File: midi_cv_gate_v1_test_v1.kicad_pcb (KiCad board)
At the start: 2 copper layers, 15 x 100 mm, 26 parts, among them J1 Conn_02x05_Odd_Even, J2 Jack1, J3 Jack2, U1 LM7805_TO220, U2 TL072

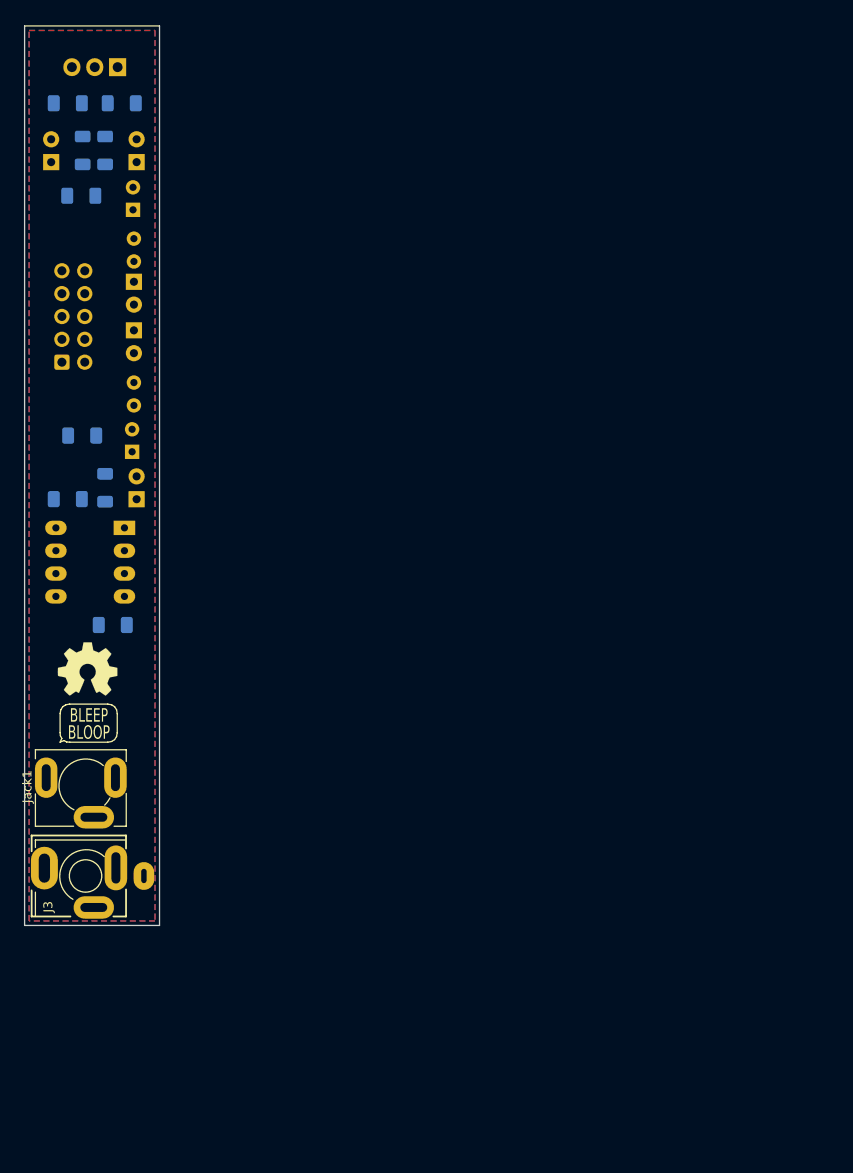
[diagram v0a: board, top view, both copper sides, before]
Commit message: Component positions first draft
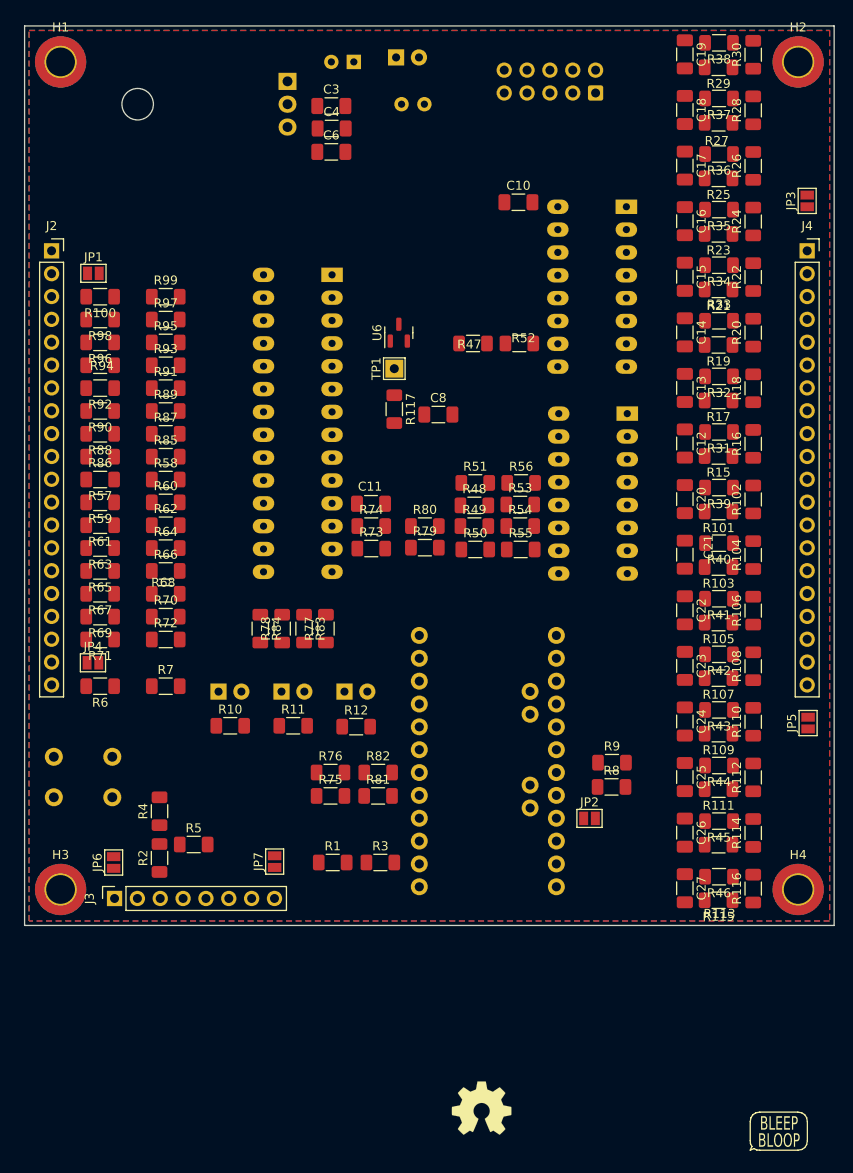
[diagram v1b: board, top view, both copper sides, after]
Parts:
- removed C2: 100uF, Capacitor_THT:CP_Radial_D5.0mm_P2.50mm
- removed C7: 10nF, Capacitor_SMD:C_1206_3216Metric_Pad1.33x1.80mm_HandSolder
- removed D2: D, Diode_THT:D_A-405_P2.54mm_Vertical_KathodeUp
- removed FB1: FerriteBead, Inductor_THT:L_Axial_L6.6mm_D2.7mm_P2.54mm_Vertical_Vishay_IM-2
- added C11: 10nF, Capacitor_SMD:C_1206_3216Metric_Pad1.33x1.80mm_HandSolder, F.Cu at (178.5, 103.1)
- added C12: 100nF, Capacitor_SMD:C_1206_3216Metric_Pad1.33x1.80mm_HandSolder, F.Cu at (213.4, 96.4)
- added C13: 100nF, Capacitor_SMD:C_1206_3216Metric_Pad1.33x1.80mm_HandSolder, F.Cu at (213.4, 90.2)
- added C14: 100nF, Capacitor_SMD:C_1206_3216Metric_Pad1.33x1.80mm_HandSolder, F.Cu at (213.4, 84.1)
- added C15: 100nF, Capacitor_SMD:C_1206_3216Metric_Pad1.33x1.80mm_HandSolder, F.Cu at (213.4, 77.9)
- added C16: 100nF, Capacitor_SMD:C_1206_3216Metric_Pad1.33x1.80mm_HandSolder, F.Cu at (213.4, 71.7)
- added C17: 100nF, Capacitor_SMD:C_1206_3216Metric_Pad1.33x1.80mm_HandSolder, F.Cu at (213.4, 65.5)
- added C18: 100nF, Capacitor_SMD:C_1206_3216Metric_Pad1.33x1.80mm_HandSolder, F.Cu at (213.4, 59.3)
- added C19: 100nF, Capacitor_SMD:C_1206_3216Metric_Pad1.33x1.80mm_HandSolder, F.Cu at (213.4, 53.2)
- added C20: 100nF, Capacitor_SMD:C_1206_3216Metric_Pad1.33x1.80mm_HandSolder, F.Cu at (213.4, 102.6)
- added C21: 100nF, Capacitor_SMD:C_1206_3216Metric_Pad1.33x1.80mm_HandSolder, F.Cu at (213.4, 108.8)
- added C22: 100nF, Capacitor_SMD:C_1206_3216Metric_Pad1.33x1.80mm_HandSolder, F.Cu at (213.4, 115.0)
- added C23: 100nF, Capacitor_SMD:C_1206_3216Metric_Pad1.33x1.80mm_HandSolder, F.Cu at (213.4, 121.1)
- added C24: 100nF, Capacitor_SMD:C_1206_3216Metric_Pad1.33x1.80mm_HandSolder, F.Cu at (213.4, 127.3)
- added C25: 100nF, Capacitor_SMD:C_1206_3216Metric_Pad1.33x1.80mm_HandSolder, F.Cu at (213.4, 133.5)
- added C26: 100nF, Capacitor_SMD:C_1206_3216Metric_Pad1.33x1.80mm_HandSolder, F.Cu at (213.4, 139.7)
- added C27: 100nF, Capacitor_SMD:C_1206_3216Metric_Pad1.33x1.80mm_HandSolder, F.Cu at (213.4, 145.9)
- added H1: MountingHole_Pad, MountingHole:MountingHole_3.2mm_M3_ISO7380_Pad_TopBottom, F.Cu at (144.0, 54.0)
- added H2: MountingHole_Pad, MountingHole:MountingHole_3.2mm_M3_ISO7380_Pad_TopBottom, F.Cu at (226.0, 54.0)
- added H3: MountingHole_Pad, MountingHole:MountingHole_3.2mm_M3_ISO7380_Pad_TopBottom, F.Cu at (144.0, 146.0)
- added H4: MountingHole_Pad, MountingHole:MountingHole_3.2mm_M3_ISO7380_Pad_TopBottom, F.Cu at (226.0, 146.0)
- added J4: Conn_01x20, Connector_PinSocket_2.54mm:PinSocket_1x20_P2.54mm_Vertical, F.Cu at (227.0, 75.0)
- added JP1: Jumper_2_Open, Jumper:SolderJumper-2_P1.3mm_Open_Pad1.0x1.5mm, F.Cu at (147.7, 77.5)
- added JP2: Jumper_2_Open, Jumper:SolderJumper-2_P1.3mm_Open_Pad1.0x1.5mm, F.Cu at (202.8, 138.1)
- added JP3: Jumper_2_Open, Jumper:SolderJumper-2_P1.3mm_Open_Pad1.0x1.5mm, F.Cu at (227.0, 69.5)
- added JP4: Jumper_2_Open, Jumper:SolderJumper-2_P1.3mm_Open_Pad1.0x1.5mm, F.Cu at (147.6, 120.8)
- added JP5: Jumper_2_Open, Jumper:SolderJumper-2_P1.3mm_Open_Pad1.0x1.5mm, F.Cu at (227.1, 127.5)
- added JP6: Jumper_2_Open, Jumper:SolderJumper-2_P1.3mm_Open_Pad1.0x1.5mm, F.Cu at (149.9, 143.0)
- added JP7: Jumper_2_Open, Jumper:SolderJumper-2_P1.3mm_Open_Pad1.0x1.5mm, F.Cu at (167.8, 142.9)
- added R10: 1k, Resistor_SMD:R_1206_3216Metric_Pad1.30x1.75mm_HandSolder, F.Cu at (162.9, 127.8)
- added R100: 10k, Resistor_SMD:R_1206_3216Metric_Pad1.30x1.75mm_HandSolder, F.Cu at (148.4, 80.1)
- added R101: 10k, Resistor_SMD:R_1206_3216Metric_Pad1.30x1.75mm_HandSolder, F.Cu at (217.2, 104.0)
- added R102: 10k, Resistor_SMD:R_1206_3216Metric_Pad1.30x1.75mm_HandSolder, F.Cu at (221.0, 102.6)
- added R103: 10k, Resistor_SMD:R_1206_3216Metric_Pad1.30x1.75mm_HandSolder, F.Cu at (217.2, 110.2)
- added R104: 10k, Resistor_SMD:R_1206_3216Metric_Pad1.30x1.75mm_HandSolder, F.Cu at (221.0, 108.8)
- added R105: 10k, Resistor_SMD:R_1206_3216Metric_Pad1.30x1.75mm_HandSolder, F.Cu at (217.2, 116.3)
- added R106: 10k, Resistor_SMD:R_1206_3216Metric_Pad1.30x1.75mm_HandSolder, F.Cu at (221.0, 115.0)
- added R107: 10k, Resistor_SMD:R_1206_3216Metric_Pad1.30x1.75mm_HandSolder, F.Cu at (217.2, 122.5)
- added R108: 10k, Resistor_SMD:R_1206_3216Metric_Pad1.30x1.75mm_HandSolder, F.Cu at (221.0, 121.2)
- added R109: 10k, Resistor_SMD:R_1206_3216Metric_Pad1.30x1.75mm_HandSolder, F.Cu at (217.2, 128.7)
- added R11: 1k, Resistor_SMD:R_1206_3216Metric_Pad1.30x1.75mm_HandSolder, F.Cu at (169.9, 127.8)
- added R110: 10k, Resistor_SMD:R_1206_3216Metric_Pad1.30x1.75mm_HandSolder, F.Cu at (221.0, 127.4)
- added R111: 10k, Resistor_SMD:R_1206_3216Metric_Pad1.30x1.75mm_HandSolder, F.Cu at (217.2, 134.9)
- added R112: 10k, Resistor_SMD:R_1206_3216Metric_Pad1.30x1.75mm_HandSolder, F.Cu at (221.0, 133.5)
- added R113: 10k, Resistor_SMD:R_1206_3216Metric_Pad1.30x1.75mm_HandSolder, F.Cu at (217.2, 141.0)
- added R114: 10k, Resistor_SMD:R_1206_3216Metric_Pad1.30x1.75mm_HandSolder, F.Cu at (221.0, 139.7)
- added R115: 10k, Resistor_SMD:R_1206_3216Metric_Pad1.30x1.75mm_HandSolder, F.Cu at (217.2, 147.2)
- added R116: 10k, Resistor_SMD:R_1206_3216Metric_Pad1.30x1.75mm_HandSolder, F.Cu at (221.0, 145.9)
- added R117: 10k, Resistor_SMD:R_1206_3216Metric_Pad1.30x1.75mm_HandSolder, F.Cu at (181.1, 92.6)
- added R12: 1k, Resistor_SMD:R_1206_3216Metric_Pad1.30x1.75mm_HandSolder, F.Cu at (176.9, 127.9)
- added R15: 10k, Resistor_SMD:R_1206_3216Metric_Pad1.30x1.75mm_HandSolder, F.Cu at (217.2, 97.8)
- added R16: 10k, Resistor_SMD:R_1206_3216Metric_Pad1.30x1.75mm_HandSolder, F.Cu at (221.0, 96.5)
- added R17: 10k, Resistor_SMD:R_1206_3216Metric_Pad1.30x1.75mm_HandSolder, F.Cu at (217.2, 91.6)
- added R18: 10k, Resistor_SMD:R_1206_3216Metric_Pad1.30x1.75mm_HandSolder, F.Cu at (221.0, 90.3)
- added R19: 10k, Resistor_SMD:R_1206_3216Metric_Pad1.30x1.75mm_HandSolder, F.Cu at (217.2, 85.5)
- added R20: 10k, Resistor_SMD:R_1206_3216Metric_Pad1.30x1.75mm_HandSolder, F.Cu at (221.0, 84.1)
- added R21: 10k, Resistor_SMD:R_1206_3216Metric_Pad1.30x1.75mm_HandSolder, F.Cu at (217.2, 79.3)
- added R22: 10k, Resistor_SMD:R_1206_3216Metric_Pad1.30x1.75mm_HandSolder, F.Cu at (221.0, 77.9)
- added R23: 10k, Resistor_SMD:R_1206_3216Metric_Pad1.30x1.75mm_HandSolder, F.Cu at (217.2, 73.1)
- added R24: 10k, Resistor_SMD:R_1206_3216Metric_Pad1.30x1.75mm_HandSolder, F.Cu at (221.0, 71.7)
- added R25: 10k, Resistor_SMD:R_1206_3216Metric_Pad1.30x1.75mm_HandSolder, F.Cu at (217.2, 66.9)
- added R26: 10k, Resistor_SMD:R_1206_3216Metric_Pad1.30x1.75mm_HandSolder, F.Cu at (221.0, 65.6)
- added R27: 10k, Resistor_SMD:R_1206_3216Metric_Pad1.30x1.75mm_HandSolder, F.Cu at (217.2, 60.8)
- added R28: 10k, Resistor_SMD:R_1206_3216Metric_Pad1.30x1.75mm_HandSolder, F.Cu at (221.0, 59.4)
- added R29: 10k, Resistor_SMD:R_1206_3216Metric_Pad1.30x1.75mm_HandSolder, F.Cu at (217.2, 54.6)
- added R30: 10k, Resistor_SMD:R_1206_3216Metric_Pad1.30x1.75mm_HandSolder, F.Cu at (221.0, 53.2)
- added R31: 330, Resistor_SMD:R_1206_3216Metric_Pad1.30x1.75mm_HandSolder, F.Cu at (217.2, 95.1)
- added R32: 330, Resistor_SMD:R_1206_3216Metric_Pad1.30x1.75mm_HandSolder, F.Cu at (217.2, 89.0)
- added R33: 330, Resistor_SMD:R_1206_3216Metric_Pad1.30x1.75mm_HandSolder, F.Cu at (217.2, 82.8)
- added R34: 330, Resistor_SMD:R_1206_3216Metric_Pad1.30x1.75mm_HandSolder, F.Cu at (217.2, 76.6)
- added R35: 330, Resistor_SMD:R_1206_3216Metric_Pad1.30x1.75mm_HandSolder, F.Cu at (217.2, 70.4)
- added R36: 330, Resistor_SMD:R_1206_3216Metric_Pad1.30x1.75mm_HandSolder, F.Cu at (217.2, 64.2)
- added R37: 330, Resistor_SMD:R_1206_3216Metric_Pad1.30x1.75mm_HandSolder, F.Cu at (217.2, 58.1)
- added R38: 330, Resistor_SMD:R_1206_3216Metric_Pad1.30x1.75mm_HandSolder, F.Cu at (217.2, 51.9)
- added R39: 330, Resistor_SMD:R_1206_3216Metric_Pad1.30x1.75mm_HandSolder, F.Cu at (217.2, 101.3)
- added R4: 10k, Resistor_SMD:R_1206_3216Metric_Pad1.30x1.75mm_HandSolder, F.Cu at (155.0, 137.3)
- added R40: 330, Resistor_SMD:R_1206_3216Metric_Pad1.30x1.75mm_HandSolder, F.Cu at (217.2, 107.5)
- added R41: 330, Resistor_SMD:R_1206_3216Metric_Pad1.30x1.75mm_HandSolder, F.Cu at (217.2, 113.7)
- added R42: 330, Resistor_SMD:R_1206_3216Metric_Pad1.30x1.75mm_HandSolder, F.Cu at (217.2, 119.9)
- added R43: 330, Resistor_SMD:R_1206_3216Metric_Pad1.30x1.75mm_HandSolder, F.Cu at (217.2, 126.0)
- added R44: 330, Resistor_SMD:R_1206_3216Metric_Pad1.30x1.75mm_HandSolder, F.Cu at (217.2, 132.2)
- added R45: 330, Resistor_SMD:R_1206_3216Metric_Pad1.30x1.75mm_HandSolder, F.Cu at (217.2, 138.4)
- added R46: 330, Resistor_SMD:R_1206_3216Metric_Pad1.30x1.75mm_HandSolder, F.Cu at (217.2, 144.6)
- added R47: 10k, Resistor_SMD:R_1206_3216Metric_Pad1.30x1.75mm_HandSolder, F.Cu at (189.8, 85.3)
- added R48: 10k, Resistor_SMD:R_1206_3216Metric_Pad1.30x1.75mm_HandSolder, F.Cu at (190.0, 103.3)
- added R49: 10k, Resistor_SMD:R_1206_3216Metric_Pad1.30x1.75mm_HandSolder, F.Cu at (190.0, 105.6)
- added R5: 10k, Resistor_SMD:R_1206_3216Metric_Pad1.30x1.75mm_HandSolder, F.Cu at (158.8, 141.0)
- added R50: 10k, Resistor_SMD:R_1206_3216Metric_Pad1.30x1.75mm_HandSolder, F.Cu at (190.1, 108.2)
- added R51: 10k, Resistor_SMD:R_1206_3216Metric_Pad1.30x1.75mm_HandSolder, F.Cu at (190.1, 100.8)
- added R52: 10k, Resistor_SMD:R_1206_3216Metric_Pad1.30x1.75mm_HandSolder, F.Cu at (195.0, 85.3)
- added R53: 10k, Resistor_SMD:R_1206_3216Metric_Pad1.30x1.75mm_HandSolder, F.Cu at (195.1, 103.2)
- added R54: 10k, Resistor_SMD:R_1206_3216Metric_Pad1.30x1.75mm_HandSolder, F.Cu at (195.1, 105.6)
- added R55: 10k, Resistor_SMD:R_1206_3216Metric_Pad1.30x1.75mm_HandSolder, F.Cu at (195.2, 108.2)
- added R56: 10k, Resistor_SMD:R_1206_3216Metric_Pad1.30x1.75mm_HandSolder, F.Cu at (195.2, 100.8)
- added R57: 10k, Resistor_SMD:R_1206_3216Metric_Pad1.30x1.75mm_HandSolder, F.Cu at (148.4, 100.4)
- added R58: 10k, Resistor_SMD:R_1206_3216Metric_Pad1.30x1.75mm_HandSolder, F.Cu at (155.7, 100.4)
- added R59: 10k, Resistor_SMD:R_1206_3216Metric_Pad1.30x1.75mm_HandSolder, F.Cu at (148.4, 103.0)
- added R6: 10k, Resistor_SMD:R_1206_3216Metric_Pad1.30x1.75mm_HandSolder, F.Cu at (148.4, 123.4)
- added R60: 10k, Resistor_SMD:R_1206_3216Metric_Pad1.30x1.75mm_HandSolder, F.Cu at (155.7, 103.0)
- added R61: 10k, Resistor_SMD:R_1206_3216Metric_Pad1.30x1.75mm_HandSolder, F.Cu at (148.4, 105.5)
- added R62: 10k, Resistor_SMD:R_1206_3216Metric_Pad1.30x1.75mm_HandSolder, F.Cu at (155.7, 105.5)
- added R63: 10k, Resistor_SMD:R_1206_3216Metric_Pad1.30x1.75mm_HandSolder, F.Cu at (148.4, 108.0)
- added R64: 10k, Resistor_SMD:R_1206_3216Metric_Pad1.30x1.75mm_HandSolder, F.Cu at (155.7, 108.0)
- added R65: 10k, Resistor_SMD:R_1206_3216Metric_Pad1.30x1.75mm_HandSolder, F.Cu at (148.4, 110.6)
- added R66: 10k, Resistor_SMD:R_1206_3216Metric_Pad1.30x1.75mm_HandSolder, F.Cu at (155.7, 110.6)
- added R67: 10k, Resistor_SMD:R_1206_3216Metric_Pad1.30x1.75mm_HandSolder, F.Cu at (148.4, 113.1)
- added R68: 10k, Resistor_SMD:R_1206_3216Metric_Pad1.30x1.75mm_HandSolder, F.Cu at (155.7, 113.1)
- added R69: 10k, Resistor_SMD:R_1206_3216Metric_Pad1.30x1.75mm_HandSolder, F.Cu at (148.4, 115.7)
- added R7: 10k, Resistor_SMD:R_1206_3216Metric_Pad1.30x1.75mm_HandSolder, F.Cu at (155.7, 123.4)
- added R70: 10k, Resistor_SMD:R_1206_3216Metric_Pad1.30x1.75mm_HandSolder, F.Cu at (155.7, 115.7)
- added R71: 10k, Resistor_SMD:R_1206_3216Metric_Pad1.30x1.75mm_HandSolder, F.Cu at (148.4, 118.2)
- added R72: 10k, Resistor_SMD:R_1206_3216Metric_Pad1.30x1.75mm_HandSolder, F.Cu at (155.7, 118.2)
- added R73: 10k, Resistor_SMD:R_1206_3216Metric_Pad1.30x1.75mm_HandSolder, F.Cu at (178.5, 108.1)
- added R74: 10k, Resistor_SMD:R_1206_3216Metric_Pad1.30x1.75mm_HandSolder, F.Cu at (178.5, 105.6)
- added R75: 10k, Resistor_SMD:R_1206_3216Metric_Pad1.30x1.75mm_HandSolder, F.Cu at (174.0, 135.6)
- added R76: 10k, Resistor_SMD:R_1206_3216Metric_Pad1.30x1.75mm_HandSolder, F.Cu at (174.0, 133.0)
- added R77: 10k, Resistor_SMD:R_1206_3216Metric_Pad1.30x1.75mm_HandSolder, F.Cu at (173.5, 117.0)
- added R78: 10k, Resistor_SMD:R_1206_3216Metric_Pad1.30x1.75mm_HandSolder, F.Cu at (168.6, 117.0)
- added R79: 10k, Resistor_SMD:R_1206_3216Metric_Pad1.30x1.75mm_HandSolder, F.Cu at (184.5, 108.0)
- added R8: 10k, Resistor_SMD:R_1206_3216Metric_Pad1.30x1.75mm_HandSolder, F.Cu at (205.2, 134.6)
- added R80: 10k, Resistor_SMD:R_1206_3216Metric_Pad1.30x1.75mm_HandSolder, F.Cu at (184.5, 105.6)
- added R81: 10k, Resistor_SMD:R_1206_3216Metric_Pad1.30x1.75mm_HandSolder, F.Cu at (179.3, 135.6)
- added R82: 10k, Resistor_SMD:R_1206_3216Metric_Pad1.30x1.75mm_HandSolder, F.Cu at (179.3, 133.0)
- added R83: 10k, Resistor_SMD:R_1206_3216Metric_Pad1.30x1.75mm_HandSolder, F.Cu at (171.1, 117.0)
- added R84: 10k, Resistor_SMD:R_1206_3216Metric_Pad1.30x1.75mm_HandSolder, F.Cu at (166.2, 117.0)
- added R85: 10k, Resistor_SMD:R_1206_3216Metric_Pad1.30x1.75mm_HandSolder, F.Cu at (155.7, 97.9)
- added R86: 10k, Resistor_SMD:R_1206_3216Metric_Pad1.30x1.75mm_HandSolder, F.Cu at (148.4, 97.9)
- added R87: 10k, Resistor_SMD:R_1206_3216Metric_Pad1.30x1.75mm_HandSolder, F.Cu at (155.7, 95.3)
- added R88: 10k, Resistor_SMD:R_1206_3216Metric_Pad1.30x1.75mm_HandSolder, F.Cu at (148.4, 95.3)
- added R89: 10k, Resistor_SMD:R_1206_3216Metric_Pad1.30x1.75mm_HandSolder, F.Cu at (155.7, 92.8)
- added R9: 10k, Resistor_SMD:R_1206_3216Metric_Pad1.30x1.75mm_HandSolder, F.Cu at (205.3, 131.9)
- added R90: 10k, Resistor_SMD:R_1206_3216Metric_Pad1.30x1.75mm_HandSolder, F.Cu at (148.4, 92.8)
- added R91: 10k, Resistor_SMD:R_1206_3216Metric_Pad1.30x1.75mm_HandSolder, F.Cu at (155.7, 90.3)
- added R92: 10k, Resistor_SMD:R_1206_3216Metric_Pad1.30x1.75mm_HandSolder, F.Cu at (148.4, 90.3)
- added R93: 10k, Resistor_SMD:R_1206_3216Metric_Pad1.30x1.75mm_HandSolder, F.Cu at (155.7, 87.7)
- added R94: 10k, Resistor_SMD:R_1206_3216Metric_Pad1.30x1.75mm_HandSolder, F.Cu at (148.4, 87.7)
- added R95: 10k, Resistor_SMD:R_1206_3216Metric_Pad1.30x1.75mm_HandSolder, F.Cu at (155.7, 85.2)
- added R96: 10k, Resistor_SMD:R_1206_3216Metric_Pad1.30x1.75mm_HandSolder, F.Cu at (148.4, 85.2)
- added R97: 10k, Resistor_SMD:R_1206_3216Metric_Pad1.30x1.75mm_HandSolder, F.Cu at (155.7, 82.6)
- added R98: 10k, Resistor_SMD:R_1206_3216Metric_Pad1.30x1.75mm_HandSolder, F.Cu at (148.4, 82.6)
- added R99: 10k, Resistor_SMD:R_1206_3216Metric_Pad1.30x1.75mm_HandSolder, F.Cu at (155.7, 80.1)
- added SW_RESET1: SW_Push, Button_Switch_THT:SW_PUSH_6mm_H5mm, B.Cu at (149.8, 131.2)
- added TP1: TestPoint, TestPoint:TestPoint_THTPad_2.0x2.0mm_Drill1.0mm, F.Cu at (181.1, 88.1)
- added U3: MCP3208, Package_DIP:DIP-16_W7.62mm_Socket_LongPads, B.Cu at (206.9, 70.1)
- added U4: MCP3208, Package_DIP:DIP-16_W7.62mm_Socket_LongPads, B.Cu at (207.0, 93.1)
- added U5: MCP23018_SP, Package_DIP:DIP-28_W7.62mm_Socket_LongPads, B.Cu at (174.2, 77.7)
- added U6: LM4040DBZ-5, Package_TO_SOT_SMD:SOT-23, F.Cu at (181.6, 84.1)
- C10: renamed from C5; value 10nF -> 100nF; moved to F.Cu
- C3, C4, C6: moved to F.Cu
- C8: value 10nF -> 100nF; moved to F.Cu
- D1: value +12_LED -> +5_LED
- D4: value -12_LED -> +5_LED
- J2: value Jack1 -> Conn_01x20; footprint My Stuff:Jack_3.5mm_MJ-355W_Vertical -> Connector_PinSocket_2.54mm:PinSocket_1x20_P2.54mm_Vertical
- J3: value Jack2 -> Conn_01x08; footprint My Stuff:Jack_3.5mm_MJ-355W_and_PJ398SM_Vertical -> Connector_PinSocket_2.54mm:PinSocket_1x08_P2.54mm_Vertical
- R1, R2, R3: value R -> 10k; moved to F.Cu
- U1: footprint Package_TO_SOT_THT:TO-220-3_Vertical -> Package_TO_SOT_THT:TO-220-3_Horizontal_TabDown
- U2: value TL072 -> ARDUINO_PRO_MINI_custom_2; footprint Package_DIP:DIP-8_W7.62mm_Socket_LongPads -> My Stuff:MODULE_ARDUINO_PRO_MINI_custom_2
- moved LOGO1 89.1 mm to (223.8, 172.9)
- moved LOGO2 89.1 mm to (223.8, 172.9)
- moved R3 85.8 mm to (179.6, 143.0), turned to 0 degrees
- moved R1 83.1 mm to (174.2, 143.0), turned to 0 degrees
- moved D5 67.3 mm to (175.6, 124.0), turned to 0 degrees
- moved J1 66.5 mm to (203.5, 57.5), turned to 90 degrees
- moved LOGO3 65.6 mm to (190.8, 170.3)
- moved J2 59.6 mm to (143.0, 75.0), turned to 0 degrees
- moved D1 59.6 mm to (161.6, 124.0), turned to 0 degrees
- moved C10 55.0 mm to (194.9, 69.6), turned to 0 degrees
- moved U2 48.7 mm to (191.5, 133.0), turned to 0 degrees
- moved C8 43.1 mm to (186.0, 93.2)
- moved R2 41.6 mm to (155.0, 142.5)
- moved D3 38.4 mm to (181.3, 53.5), turned to 0 degrees
- moved FB2 33.3 mm to (181.9, 58.7), turned to 0 degrees
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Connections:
- C10 pad 2: -12V -> +5V
- C8 pad 2: -12V -> +5V
- D1 pad 2: +12V -> Net-(D1-Pad2)
- D4 pad 2: GND -> Net-(D4-Pad2)
- D5 pad 2: +5V -> Net-(D5-Pad2)
- J1 pad 1: -12VA -> unconnected-(J1-Pad1)
- J1 pad 2: -12VA -> unconnected-(J1-Pad2)
- R1 pad 1: Net-(D1-Pad1) -> +5V
- R1 pad 2: GND -> Net-(J3-Pad2)
- R2 pad 1: Net-(D4-Pad1) -> +5V
- R2 pad 2: -12V -> Net-(J3-Pad3)
- R3 pad 1: Net-(D5-Pad1) -> Net-(J3-Pad2)
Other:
- board size 15 x 100 mm -> 90 x 100 mm
- board text removed: "Eurorack Template"

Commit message: First pass routing done
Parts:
- added JP8: Jumper_2_Open, Jumper:SolderJumper-2_P1.3mm_Open_Pad1.0x1.5mm, F.Cu at (187.5, 89.8)
- JP5: moved to B.Cu
- moved R117 10.9 mm to (184.4, 82.2), turned to 90 degrees
- moved C8 9.10 mm to (195.1, 93.1)
- moved U6 6.96 mm to (183.5, 90.8), turned to -90 degrees
- moved R81 6.18 mm to (174.1, 138.9), turned to 180 degrees
- moved R82 5.41 mm to (174.1, 134.3), turned to 180 degrees
- moved JP7 5.26 mm to (171.1, 147.0), turned to -90 degrees
- moved TP1 3.64 mm to (184.4, 86.5), turned to 0 degrees
- moved R8 3.11 mm to (205.2, 131.5), turned to 90 degrees
- moved R9 2.88 mm to (202.5, 131.4), turned to 90 degrees
- moved R99 2.79 mm to (155.7, 77.3)
- moved R79 2.59 mm to (184.4, 110.6)
- moved R73 2.52 mm to (178.5, 110.6)
- moved R97 2.45 mm to (155.7, 80.2)
- moved R56 2.42 mm to (195.2, 98.4)
- moved R51 2.42 mm to (190.1, 98.4)
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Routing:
- net +5V: track 0.00 -> 352.2 mm, vias 0 -> 23
- net +12V: track 0.00 -> 330.9 mm, vias 0 -> 2
- net Net-(R6-Pad1): track 0.00 -> 84.2 mm, vias 0 -> 5
- net /analog_inputs/~{CS}/SHDN_0: track 0.00 -> 67.6 mm, vias 0 -> 2
- net INT1: track 0.00 -> 67.0 mm, vias 0 -> 3
- net INT0: track 0.00 -> 64.5 mm, vias 0 -> 2
- net /analog_inputs/CLK: track 0.00 -> 62.4 mm, vias 0 -> 2
- net /analog_inputs/Dout: track 0.00 -> 59.5 mm, vias 0 -> 3
- net Net-(J3-Pad2): track 0.00 -> 57.7 mm, vias 0 -> 3
- net /analog_inputs/Din: track 0.00 -> 56.1 mm, vias 0 -> 3
- net /digital_io/SCL: track 0.00 -> 55.9 mm, vias 0 -> 1
- net +5VA: track 0.00 -> 54.1 mm
- net /digital_io/~{RESET}: track 0.00 -> 53.5 mm, vias 0 -> 3
- net Net-(SW_RESET1-Pad1): track 0.00 -> 48.8 mm, vias 0 -> 2
- net /digital_io/SDA: track 0.00 -> 47.1 mm, vias 0 -> 1
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
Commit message: Geographic re-annotate
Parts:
- renumbered C3 to C1, C16 to C10, C1 to C101, C15 to C11, C14 to C12, C12 to C14, C20 to C15, C21 to C16, C22 to C17, C23 to C18, C24 to C19, C4 to C2, C25 to C20, C26 to C21, C27 to C22, C6 to C3, C11 to C4, C10 to C5, C8 to C6, C19 to C7, C18 to C8, C17 to C9, D3 to D100, D5 to D101, D4 to D102, D1 to D103, FB2 to FB100, H3 to H2, H2 to H3, J2 to J1, J1 to J101, J3 to J2, J4 to J3, JP5 to JP101, JP4 to JP2, JP6 to JP3, JP7 to JP4, JP8 to JP5, JP2 to JP6, JP3 to JP7, LOGO3 to LOGO1, LOGO1 to LOGO2, LOGO2 to LOGO3, R100 to R1, R59 to R10, R30 to R100, R28 to R101, R26 to R102, R24 to R103, R22 to R104, R20 to R105, R18 to R106, R16 to R107, R102 to R108, R104 to R109, R61 to R11, R106 to R110, R108 to R111, R110 to R112, R112 to R113, R116 to R115, R63 to R12, R65 to R13, R67 to R14, R69 to R15, R71 to R16, R6 to R17, R4 to R18, R2 to R19, R98 to R2, R99 to R20, R97 to R21, R95 to R22, R93 to R23, R91 to R24, R89 to R25, R87 to R26, R85 to R27, R58 to R28, R60 to R29, R96 to R3, R62 to R30, R64 to R31, R66 to R32, R68 to R33, R70 to R34, R72 to R35, R7 to R36, R5 to R37, R10 to R38, R84 to R39, R94 to R4, R78 to R40, R11 to R41, R83 to R42, R77 to R43, R76 to R44, R82 to R45, R75 to R46, R81 to R47, R1 to R48, R12 to R49, R92 to R5, R74 to R50, R73 to R51, R3 to R52, R117 to R53, R80 to R54, R79 to R55, R47 to R56, R51 to R57, R48 to R58, R49 to R59, R90 to R6, R50 to R60, R52 to R61, R56 to R62, R53 to R63, R54 to R64, R55 to R65, R9 to R66, R8 to R67, R38 to R68, R29 to R69, R88 to R7, R37 to R70, R27 to R71, R36 to R72, R25 to R73, R35 to R74, R23 to R75, R34 to R76, R21 to R77, R33 to R78, R19 to R79, R86 to R8, R32 to R80, R17 to R81, R31 to R82, R15 to R83, R39 to R84, R101 to R85, R40 to R86, R103 to R87, R41 to R88, R105 to R89, R57 to R9, R42 to R90, R107 to R91, R43 to R92, R109 to R93, R44 to R94, R111 to R95, R45 to R96, R113 to R97, R46 to R98, R115 to R99, SW_RESET1 to SW_RESET100, U6 to U1, U3 to U101, U4 to U102, U2 to U103, U5 to U104, U1 to U105

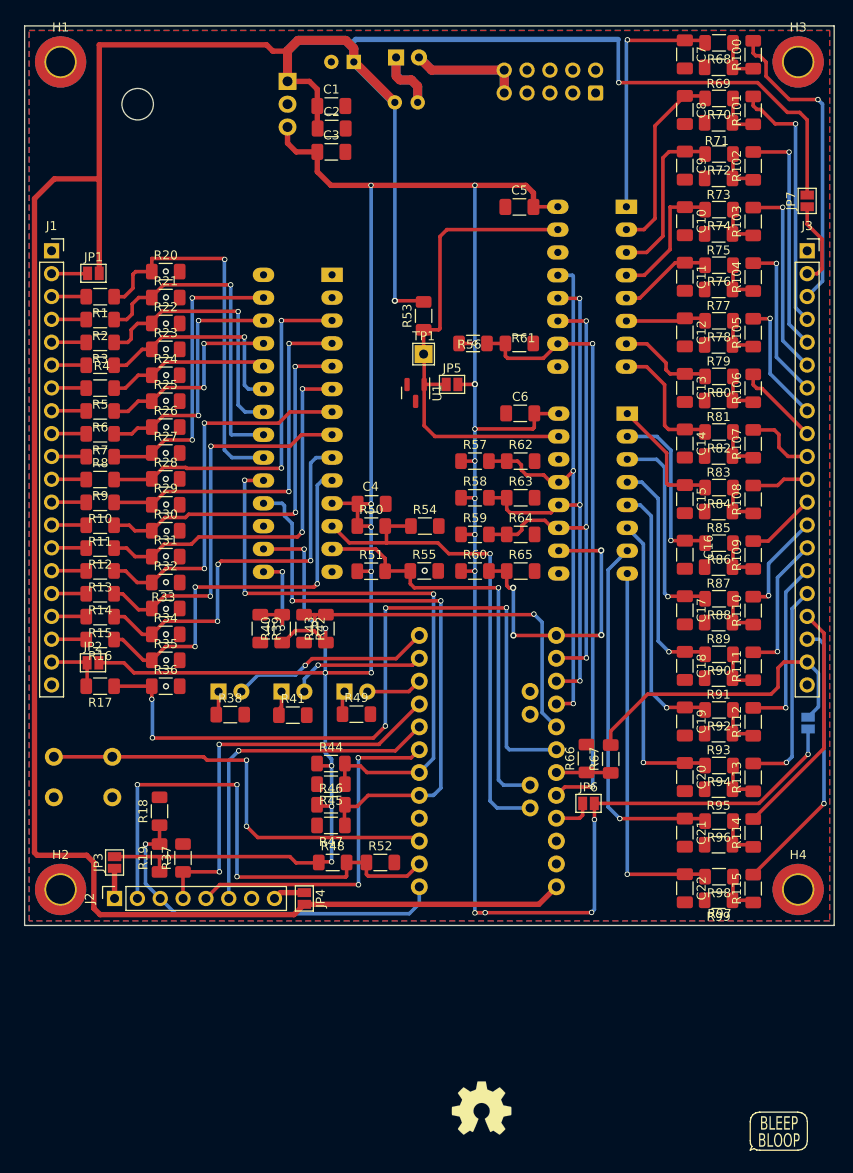
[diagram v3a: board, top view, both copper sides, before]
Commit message: Silkscreen cleanup and title block filled
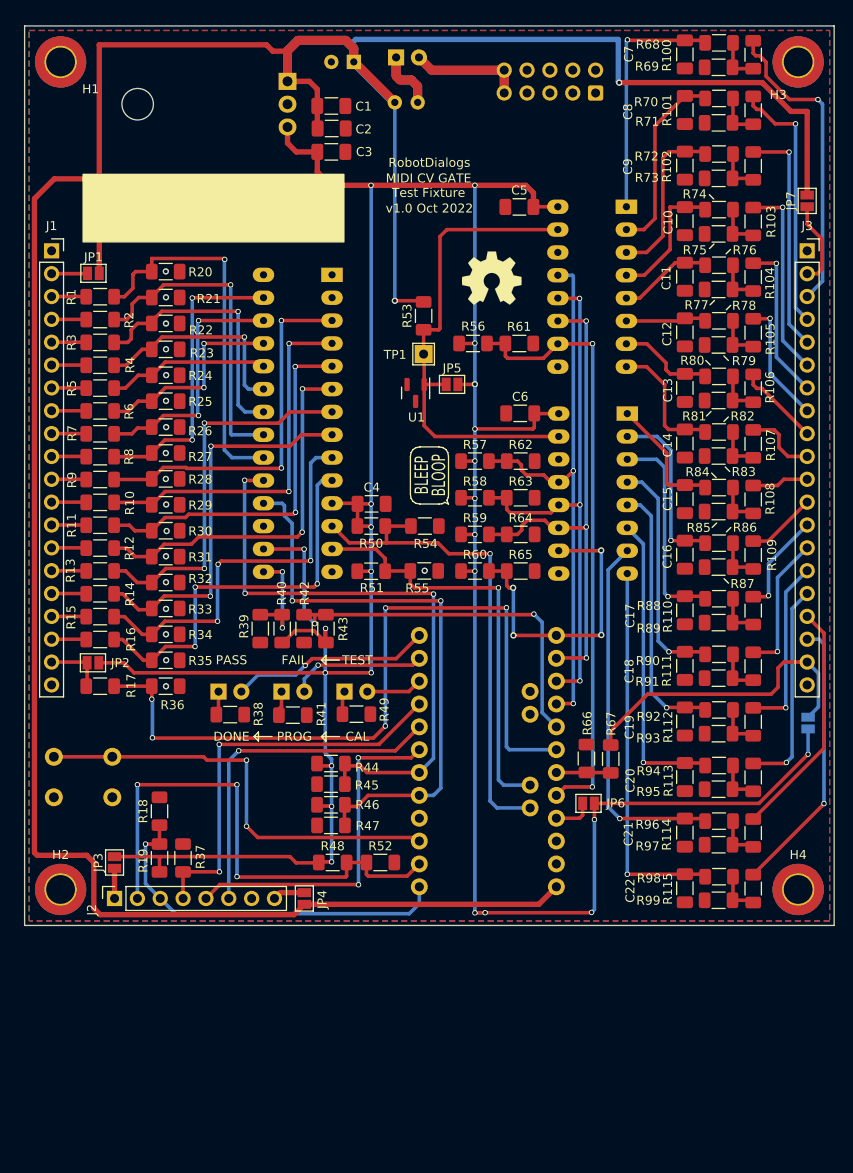
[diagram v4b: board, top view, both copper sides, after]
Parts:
- moved LOGO1 92.3 mm to (191.9, 78.0)
- moved LOGO2 82.6 mm to (185.0, 100.0), turned to 90 degrees
- moved LOGO3 82.6 mm to (185.0, 100.0)
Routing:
- net +12V: track 330.9 -> 331.4 mm
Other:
- board text added: "+12V"
- board text added: "+5V"
- board text added: "ANALOG 0"
- board text added: "ANALOG 1"
- board text added: "ANALOG 10"
- board text added: "ANALOG 11"
- board text added: "ANALOG 12"
- board text added: "ANALOG 13"
- board text added: "ANALOG 14"
- board text added: "ANALOG 15"
- board text added: "ANALOG 2"
- board text added: "ANALOG 3"
- board text added: "ANALOG 4"
- board text added: "ANALOG 5"
- board text added: "ANALOG 6"
- board text added: "ANALOG 7"
- board text added: "ANALOG 8"
- board text added: "ANALOG 9"
- board text added: "CAL"
- board text added: "DIGITAL 0"
- board text added: "DIGITAL 1"
- board text added: "DIGITAL 10"
- board text added: "DIGITAL 11"
- board text added: "DIGITAL 12"
- board text added: "DIGITAL 13"
- board text added: "DIGITAL 14"
- board text added: "DIGITAL 15"
- board text added: "DIGITAL 2"
- board text added: "DIGITAL 3"
- board text added: "DIGITAL 4"
- board text added: "DIGITAL 5"
- board text added: "DIGITAL 6"
- board text added: "DIGITAL 7"
- board text added: "DIGITAL 8"
- board text added: "DIGITAL 9"
- board text added: "DONE"
- board text added: "FAIL"
- board text added: "LED"
- board text added: "LM7805"
- board text added: "MCP23018"
- board text added: "MCP3208"
- board text added: "MIDI CV GATE Test Fixture"
- board text added: "MIDI IN"
- board text added: "MIDI OUT"
- board text added: "PASS"
- board text added: "PROG"
- board text added: "RESET"
- board text added: "SWITCH"
- board text added: "TEST"
- board text added: "v1.0 Oct 2022"
- board text removed: "v1.1 July 2022"
